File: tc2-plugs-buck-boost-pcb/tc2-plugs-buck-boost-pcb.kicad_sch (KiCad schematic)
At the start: 61 parts, among them J201 JCON_M16_04Pin, J202 JCON_M16_2+4Pin, J203 Conn_02x06_Odd_Even, Q1 Q_PMOS_GSD, Q201 Q_PMOS_GSD, Q203 AO3400A, U201 TPS63070RNMR, U201 TPS63071

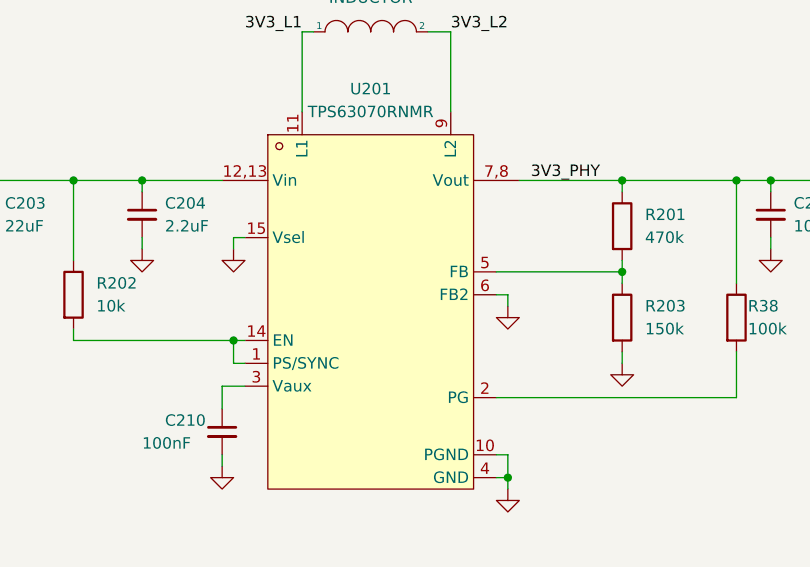
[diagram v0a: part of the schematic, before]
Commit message: Fixed panel tabs
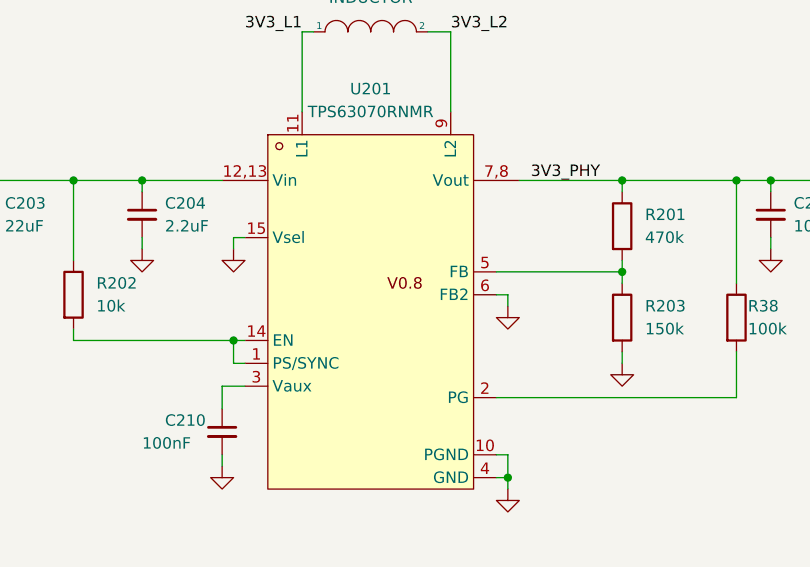
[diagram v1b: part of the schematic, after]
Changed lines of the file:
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@@
 			)
 		)
-		(property "Datasheet" "https://lcsc.com/product-detail/DC-DC-Converters_TI_TPS63070RNMR_TPS63070RNMR_C109322.html"
+		(property "Datasheet" "https://www.ti.com/lit/ds/symlink/tps63070.pdf?HQS=dis-dk-null-digikeymode-dsf-pf-null-wwe&ts=1731997103101"
 			(at 273.05 133.35 0)
 			(effects

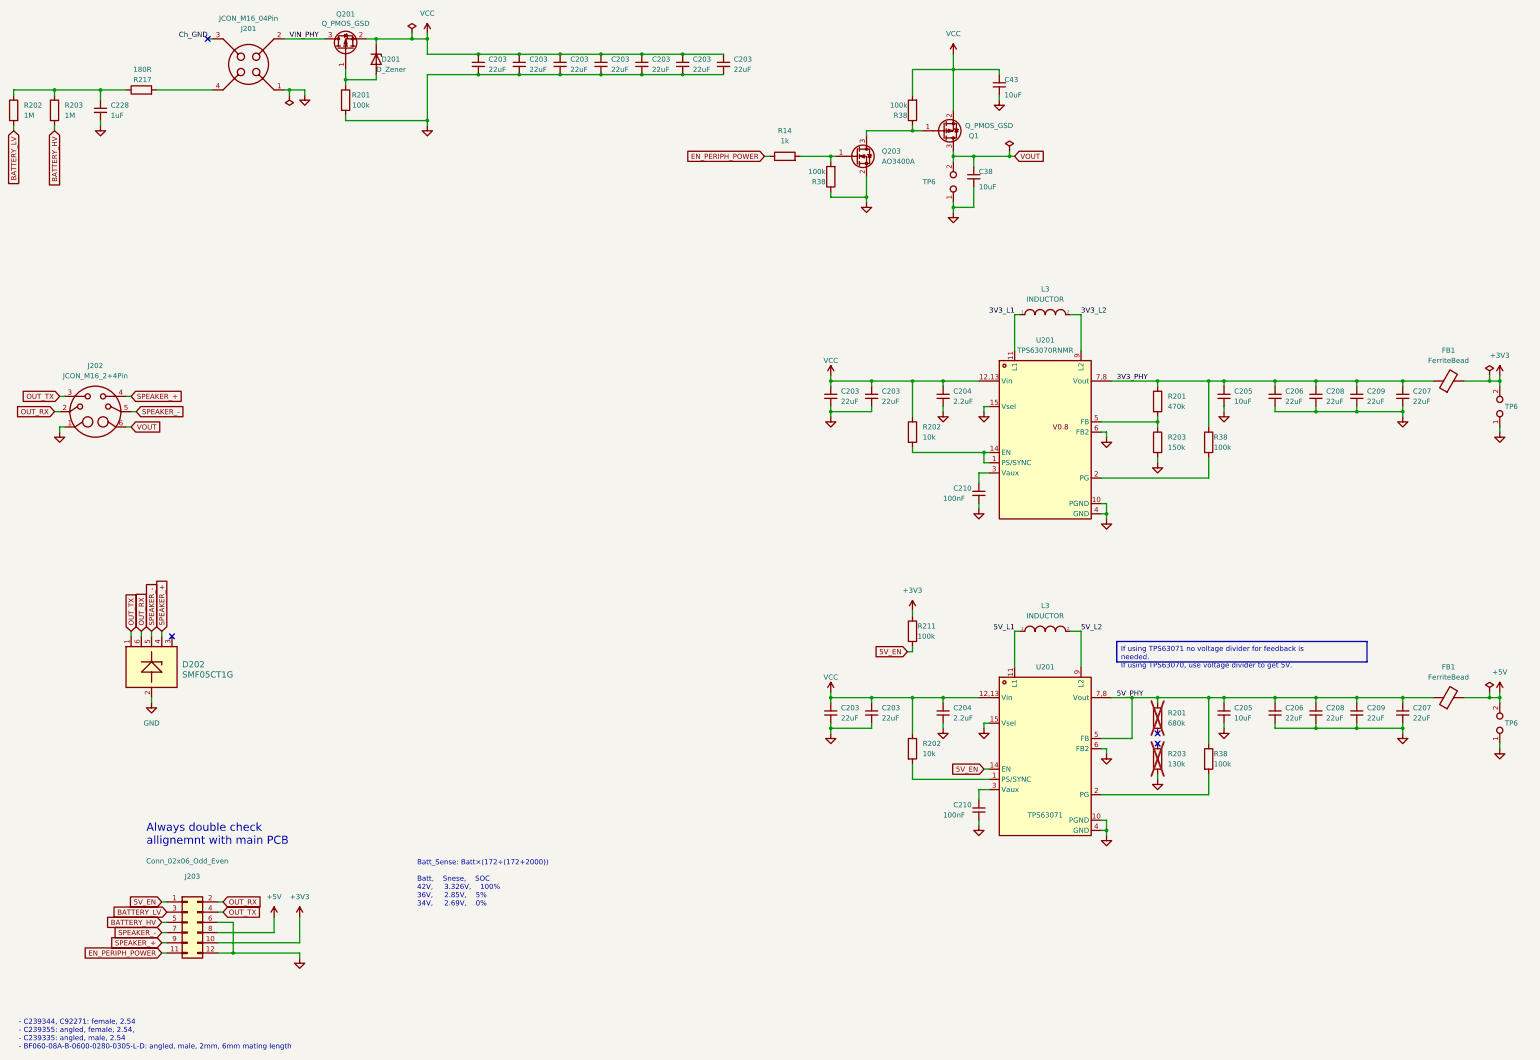
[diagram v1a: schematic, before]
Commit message: Upgraded to new kicad version
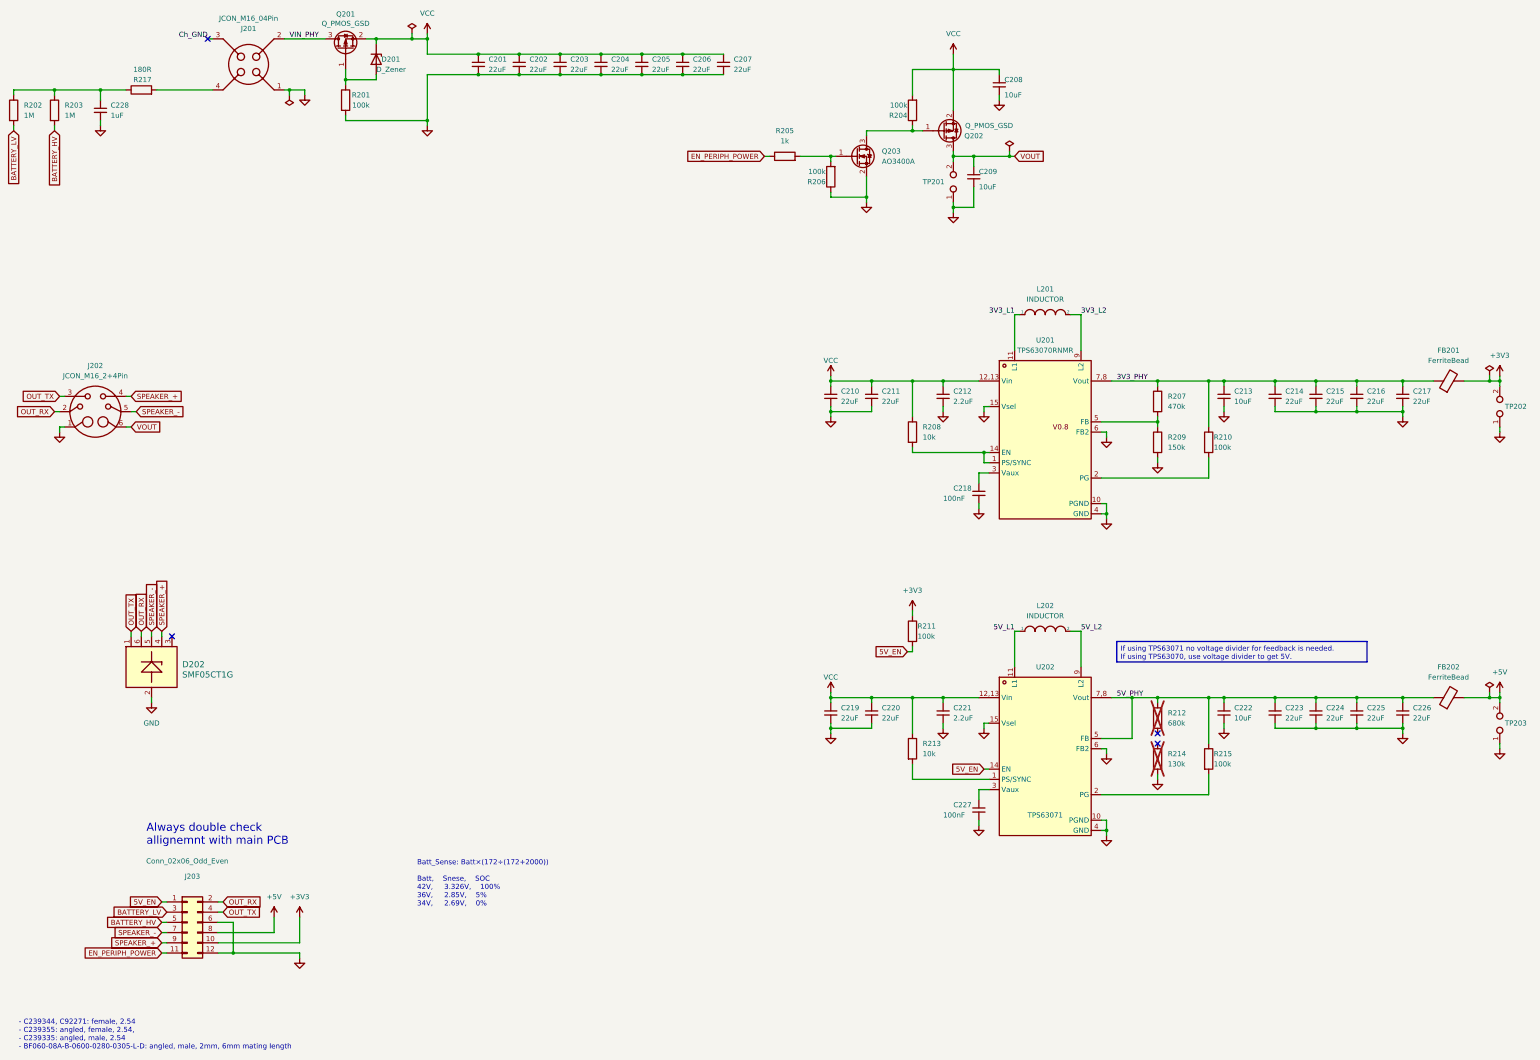
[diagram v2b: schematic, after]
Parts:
- D202: LCSC Part (none) -> C15879
- Q201: symbol Device:Q_PMOS_GSD -> Transistor_FET:Q_PMOS_GSD
- Q202: renamed from Q1; symbol Device:Q_PMOS_GSD -> Transistor_FET:Q_PMOS_GSD
- renumbered C203 to C201, C203 to C202, C203 to C204, C203 to C205, C203 to C206, C203 to C207, C43 to C208, C38 to C209, C203 to C210, C203 to C211, C204 to C212, C205 to C213, C206 to C214, C208 to C215, C209 to C216, C207 to C217, C210 to C218, C203 to C219, C203 to C220, C204 to C221, C205 to C222, C206 to C223, C208 to C224, C209 to C225, C207 to C226, C210 to C227, FB1 to FB201, FB1 to FB202, L3 to L201, L3 to L202, R38 to R204, R14 to R205, R38 to R206, R201 to R207, R202 to R208, R203 to R209, R38 to R210, R201 to R212, R202 to R213, R203 to R214, R38 to R215, TP6 to TP201, TP6 to TP202, TP6 to TP203, U201 to U202

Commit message: Tidy up for making an order for v0.7.3
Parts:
- C201, C202, C203, C204, C205, C206, C207, C210, C211, C219, C220: LCSC C45783 -> (none); LCSC Part (none) -> C45783
- C208, C209: LCSC C19702 -> (none); LCSC Part (none) -> C19702
- C212, C221: LCSC C159814 -> (none); LCSC Part (none) -> C159814
- C213, C222: LCSC C15525 -> (none); LCSC Part (none) -> C15525
- C214, C215, C216, C217, C223, C224, C225, C226: LCSC C86295 -> (none); LCSC Part (none) -> C86295
- C218, C227: LCSC C100072 -> (none); LCSC Part (none) -> C100072
- C228: LCSC C13832 -> (none); LCSC Part (none) -> C13832
- D201: LCSC C7497481 -> (none); LCSC Part (none) -> C7497481
- D202: LCSC C15879 -> (none)
- FB201, FB202: LCSC C76818 -> (none); LCSC Part (none) -> C76818
- J203: LCSC C7086099 -> (none); LCSC Part (none) -> C7086099
- L201, L202: LCSC C5179452 -> (none); LCSC Part (none) -> C5179452
- Q201, Q202: LCSC C15127 -> (none); LCSC Part (none) -> C15127
- Q203: LCSC C20917 -> (none); LCSC Part (none) -> C20917
- R201, R204, R206, R210, R211, R215: LCSC C25741 -> (none); LCSC Part (none) -> C25741
- R202, R203: LCSC C326730 -> (none); LCSC Part (none) -> C326730
- R205: LCSC C11702 -> (none); LCSC Part (none) -> C11702
- R207: LCSC C319591 -> (none); LCSC Part (none) -> C319591
- R208, R213: LCSC C25744 -> (none); LCSC Part (none) -> C25744
- R209: LCSC C723770 -> (none); LCSC Part (none) -> C723770
- R217: value 180R -> 180Ω; LCSC C38941 -> (none); LCSC Part (none) -> C38941
- U201: LCSC C109322 -> (none)
- U202: LCSC C2876599 -> (none); LCSC Part C2876599 -> C2876599
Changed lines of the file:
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@@
 			)
 		)
-		(property "LCSC" "C15525"
+		(property "LCSC Part" "C15525"
 			(at 317.5 111.76 0)
 			(effects
@@
 			)
 		)
-		(property "LCSC" "C45783"
+		(property "LCSC Part" "C45783"
 			(at 142.24 29.21 0)
 			(effects
@@
 			)
 		)
-		(property "LCSC" "C723770"
+		(property "LCSC Part" "C723770"
 			(at 300.99 123.19 0)
 			(effects
@@
 			)
 		)
-		(property "LCSC" "C13832"
+		(property "LCSC Part" "C13832"
 			(at 38.1 40.64 0)
 			(effects
@@
 			)
 		)
-		(property "LCSC" "C45783"
+		(property "LCSC Part" "C45783"
 			(at 132.08 29.21 0)
 			(effects
@@
 			)
 		)
-		(property "LCSC" "C15127"
+		(property "LCSC Part" "C15127"
 			(at 99.06 25.4 0)
 			(effects
@@
 			)
 		)
-		(property "LCSC" "C76818"
+		(property "LCSC Part" "C76818"
 			(at 373.38 186.69 0)
 			(effects
@@
 			)
 		)
-		(property "LCSC" "C7086099"
+		(property "LCSC Part" "C7086099"
 			(at 59.69 242.57 0)
 			(effects
@@
 			)
 		)
-		(property "LCSC" "C2876599 "
+		(property "LCSC Part" "C2876599 "
 			(at 273.05 193.04 0)
 			(effects
@@
 			)
 		)
-		(property "LCSC" "C100072"
+		(property "LCSC Part" "C100072"
 			(at 256.54 214.63 0)
 			(effects
@@
 			)
 		)
-		(property "LCSC" "C25741"
+		(property "LCSC Part" "C25741"
 			(at 313.69 123.19 0)
 			(effects
@@
 			)
 		)
-		(property "LCSC" "C159814"
+		(property "LCSC Part" "C159814"
 			(at 247.65 111.76 0)
 			(effects
@@
 			)
 		)
-		(property "LCSC" "C86295"
+		(property "LCSC Part" "C86295"
 			(at 350.52 190.5 0)
 			(effects
@@
 			)
 		)
-		(property "LCSC" "C45783"
+		(property "LCSC Part" "C45783"
 			(at 219.71 111.76 0)
 			(effects
@@
 			)
 		)
-		(property "LCSC" "C86295"
+		(property "LCSC Part" "C86295"
 			(at 330.2 111.76 0)
 			(effects
@@
 			)
 		)
-		(property "LCSC" "C109322"
+		(property "LCSC Part" "C109322"
 			(at 273.05 114.3 0)
 			(effects
@@
 			)
 		)
-		(property "LCSC" ""
+		(property "LCSC Part" ""
 			(at 300.99 201.93 0)
 			(effects
@@
 			)
 		)
-		(property "LCSC" "C76818"
+		(property "LCSC Part" "C76818"
 			(at 373.38 107.95 0)
 			(effects
@@
 			)
 		)
-		(property "LCSC" "C7497481"
+		(property "LCSC Part" "C7497481"
 			(at 106.68 27.94 0)
 			(effects
@@
 			)
 		)
-		(property "LCSC" "C45783"
+		(property "LCSC Part" "C45783"
 			(at 152.4 29.21 0)
 			(effects
@@
 			)
 		)
-		(property "LCSC" "C86295"
+		(property "LCSC Part" "C86295"
 			(at 361.95 111.76 0)
 			(effects
@@
 			)
 		)
-		(property "LCSC" "C86295"
+		(property "LCSC Part" "C86295"
 			(at 330.2 190.5 0)
 			(effects
@@
 			)
 		)
-		(property "Value" "180R"
+		(property "Value" "180Ω"
 			(at 50.8 30.48 90)
 			(effects
@@
 			)
 		)
-		(property "LCSC" "C38941"
+		(property "LCSC Part" "C38941"
 			(at 48.26 35.56 0)
 			(effects
@@
 			)
 		)
-		(property "LCSC" "C45783"
+		(property "LCSC Part" "C45783"
 			(at 182.88 29.21 0)
 			(effects
@@
 			)
 		)
-		(property "LCSC" "C25741"
+		(property "LCSC Part" "C25741"
 			(at 99.06 38.1 0)
 			(effects
@@
 			)
 		)
-		(property "LCSC" "C15879"
+		(property "LCSC Part" "C15879"
 			(at 50.8 177.8 0)
 			(effects
@@
 			)
 		)
-		(property "LCSC" "C326730"
+		(property "LCSC Part" "C326730"
 			(at 26.67 40.64 0)
 			(effects
@@
 			)
 		)
-		(property "LCSC" "C45783"
+		(property "LCSC Part" "C45783"
 			(at 219.71 190.5 0)
 			(effects
@@
 			)
 		)
-		(property "LCSC" "C86295"
+		(property "LCSC Part" "C86295"
 			(at 340.36 111.76 0)
 			(effects
@@
 			)
 		)
-		(property "LCSC" "C86295"
+		(property "LCSC Part" "C86295"
 			(at 340.36 190.5 0)
 			(effects
@@
 			)
 		)
-		(property "LCSC" ""
+		(property "LCSC Part" ""
 			(at 300.99 191.77 0)
 			(effects
@@
 			)
 		)
-		(property "LCSC" "C159814"
+		(property "LCSC Part" "C159814"
 			(at 247.65 190.5 0)
 			(effects
@@
 			)
 		)
-		(property "LCSC" "C25741"
+		(property "LCSC Part" "C25741"
 			(at 240.03 170.18 0)
 			(effects
@@
 			)
 		)
-		(property "LCSC" "C45783"
+		(property "LCSC Part" "C45783"
 			(at 193.04 29.21 0)
 			(effects
@@
 			)
 		)
-		(property "LCSC" "C45783"
+		(property "LCSC Part" "C45783"
 			(at 229.87 111.76 0)
 			(effects
@@
 			)
 		)
-		(property "LCSC" "C15525"
+		(property "LCSC Part" "C15525"
 			(at 317.5 190.5 0)
 			(effects
@@
 			)
 		)
-		(property "LCSC" "C20917"
+		(property "LCSC Part" "C20917"
 			(at 226.06 52.07 0)
 			(effects
@@
 			)
 		)
-		(property "LCSC" "C11702"
+		(property "LCSC Part" "C11702"
 			(at 208.28 52.07 90)
 			(effects
@@
 			)
 		)
-		(property "LCSC" "C100072"
+		(property "LCSC Part" "C100072"
 			(at 256.54 135.89 0)
 			(effects
@@
 			)
 		)
-		(property "LCSC" "C25744"
+		(property "LCSC Part" "C25744"
 			(at 240.03 120.65 0)
 			(effects
@@
 			)
 		)
-		(property "LCSC" "C326730"
+		(property "LCSC Part" "C326730"
 			(at 16.51 40.64 0)
 			(effects
@@
 			)
 		)
-		(property "LCSC" "C19702"
+		(property "LCSC Part" "C19702"
 			(at 255.27 57.15 0)
 			(effects
@@
 			)
 		)
-		(property "LCSC" "C319591"
+		(property "LCSC Part" "C319591"
 			(at 300.99 113.03 0)
 			(effects
@@
 			)
 		)
-		(property "LCSC" "C25741"
+		(property "LCSC Part" "C25741"
 			(at 240.03 40.64 0)
 			(effects
@@
 			)
 		)
-		(property "LCSC" "C25741"
+		(property "LCSC Part" "C25741"
 			(at 219.71 57.15 0)
 			(effects
@@
 			)
 		)
-		(property "LCSC" "C25744"
+		(property "LCSC Part" "C25744"
 			(at 240.03 199.39 0)
 			(effects
@@
 			)
 		)
-		(property "LCSC" "C5179452"
+		(property "LCSC Part" "C5179452"
 			(at 273.05 170.18 0)
 			(effects
@@
 			)
 		)
-		(property "LCSC" "C45783"
+		(property "LCSC Part" "C45783"
 			(at 172.72 29.21 0)
 			(effects
@@
 			)
 		)
-		(property "LCSC" "C25741"
+		(property "LCSC Part" "C25741"
 			(at 313.69 201.93 0)
 			(effects
@@
 			)
 		)
-		(property "LCSC" "C86295"
+		(property "LCSC Part" "C86295"
 			(at 350.52 111.76 0)
 			(effects
@@
 			)
 		)
-		(property "LCSC" "C19702"
+		(property "LCSC Part" "C19702"
 			(at 261.62 34.29 0)
 			(effects
@@
 			)
 		)
-		(property "LCSC" "C45783"
+		(property "LCSC Part" "C45783"
 			(at 162.56 29.21 0)
 			(effects
@@
 			)
 		)
-		(property "LCSC" "C15127"
+		(property "LCSC Part" "C15127"
 			(at 247.65 45.72 0)
 			(effects
@@
 			)
 		)
-		(property "LCSC" "C5179452"
+		(property "LCSC Part" "C5179452"
 			(at 273.05 91.44 0)
 			(effects
@@
 			)
 		)
-		(property "LCSC" "C45783"
+		(property "LCSC Part" "C45783"
 			(at 229.87 190.5 0)
 			(effects
@@
 			)
 		)
-		(property "LCSC" "C86295"
+		(property "LCSC Part" "C86295"
 			(at 361.95 190.5 0)
 			(effects
